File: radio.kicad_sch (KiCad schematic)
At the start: 24 parts, among them U401 CC1101RGPR, Y401 27MHz

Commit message: :memo: updated schemati and pcb information
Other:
- company: Ouroboros Embedded Education -> Ouroboros Embedded Development
- title: Project Antares - Receiver -> Project Antares - Receiver Schematic
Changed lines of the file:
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@@
 	(paper "A4")
 	(title_block
-		(title "Project Antares - Receiver")
-		(date "2024-08-22")
-		(rev "Rev 1")
-		(company "Ouroboros Embedded Education")
+		(title "Project Antares - Receiver Schematic")
+		(date "2024-08-23")
+		(rev "1.0.0")
+		(company "Ouroboros Embedded Development")
 		(comment 1 "Pablo Jean Rozario")
 	)

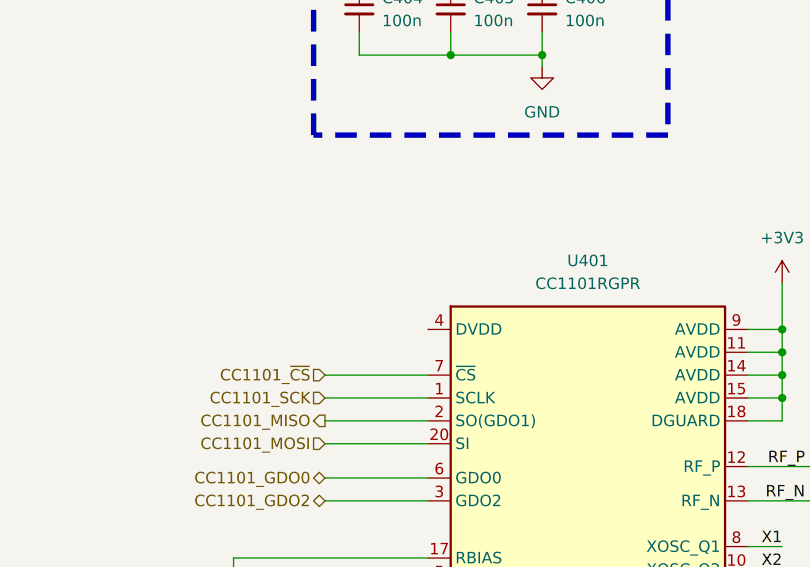
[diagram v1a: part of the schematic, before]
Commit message: :minidisc: fixed dvdd of cc1101 pin unconnected
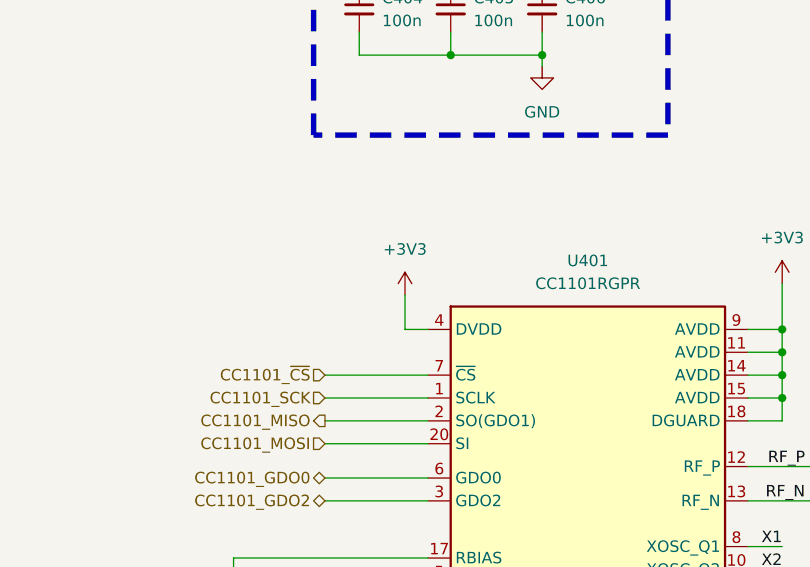
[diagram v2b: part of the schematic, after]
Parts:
- R401: LCSC C114630 -> C23206; PN RC0603FR-0756KL -> 0603WAF5602T5E
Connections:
- net +3V3: now also U401.4 (DVDD)
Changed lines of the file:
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@@
 	(title_block
 		(title "Project Antares - Receiver Schematic")
-		(date "2024-08-23")
-		(rev "1.0.0")
+		(date "2024-08-24")
+		(rev "1.0.1")
 		(company "Ouroboros Embedded Development")
 		(comment 1 "Pablo Jean Rozario")
@@
 	(wire
 		(pts
+			(xy 120.65 88.9) (xy 118.11 88.9)
+		)
+		(stroke
+			(width 0)
+			(type default)
+		)
+	)
+	(wire
+		(pts
 			(xy 116.84 121.92) (xy 120.65 121.92)
 		)
@@
 		(pts
 			(xy 109.22 107.95) (xy 120.65 107.95)
+		)
+		(stroke
+			(width 0)
+			(type default)
+		)
+	)
+	(wire
+		(pts
+			(xy 118.11 88.9) (xy 118.11 85.09)
 		)
 		(stroke
@@
 	)
 	(symbol
+		(lib_id "power:+3V3")
+		(at 118.11 85.09 0)
+		(unit 1)
+		(exclude_from_sim no)
+		(in_bom yes)
+		(on_board yes)
+		(dnp no)
+		(fields_autoplaced yes)
+		(property "Reference" "#PWR0403"
+			(at 118.11 88.9 0)
+			(effects
+				(font
+					(size 1.27 1.27)
+				)
+				(hide yes)
+			)
+		)
+		(property "Value" "+3V3"
+			(at 118.11 80.01 0)
+			(effects
+				(font
+					(size 1.27 1.27)
+				)
+			)
+		)
+		(property "Footprint" ""
+			(at 118.11 85.09 0)
+			(effects
+				(font
+					(size 1.27 1.27)
+				)
+				(hide yes)
+			)
+		)
+		(property "Datasheet" ""
+			(at 118.11 85.09 0)
+			(effects
+				(font
+					(size 1.27 1.27)
+				)
+				(hide yes)
+			)
+		)
+		(property "Description" "Power symbol creates a global label with name \"+3V3\""
+			(at 118.11 85.09 0)
+			(effects
+				(font
+					(size 1.27 1.27)
+				)
+				(hide yes)
+			)
+		)
+		(pin "1"
+		)
+		(instances
+			(project "Anteres-Receiver"
+				(path "/913f19a9-8bde-4f1b-98e5-ff93dc166c2f/3dac5b74-5ae0-4a49-abdb-9165c94eab1b"
+					(reference "#PWR0403")
+					(unit 1)
+				)
+			)
+		)
+	)
+	(symbol
 		(lib_id "Device:R_Small_US")
 		(at 99.06 120.65 0)
@@
 			)
 		)
-		(property "LCSC" "C114630"
+		(property "LCSC" "C23206"
 			(at 99.06 120.65 0)
 			(effects
@@
 			)
 		)
-		(property "PN" "RC0603FR-0756KL"
+		(property "PN" "0603WAF5602T5E"
 			(at 99.06 120.65 0)
 			(effects
